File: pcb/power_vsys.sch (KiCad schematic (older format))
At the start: 36 parts

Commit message: Stephanie fixes, net names
Removed duplicate global I2C pull-ups
Added missing BMP280 pin 7
Correcting pin names etc. on LM4120 voltage reference
Finished standardizing net names
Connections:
- net labels added: 12Vout, LM5141-AGND, LM5141-VCC, LM5141-VDDA, VLogic, VSys-En, Vin
- net labels removed: 12VOUT, LM5141_AGND, LM5141_VCC, LM5141_VDDA, VIN, VLOGIC, VSYS_EN
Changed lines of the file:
@@
 12.5-16.8V IN
 Text HLabel 2750 1350 0    50   Input ~ 0
-VIN
+Vin
 Text HLabel 8700 1350 2    50   Output ~ 0
-12VOUT
+12Vout
 Wire Wire Line
 	8400 1350 8700 1350
@@
 	5250 1800 5750 1800
 Text Label 5750 1800 2    50   ~ 0
-LM5141_VCC
+LM5141-VCC
 Text Label 7700 4200 2    50   ~ 0
-LM5141_VCC
+LM5141-VCC
 Wire Wire Line
 	6450 4200 8050 4200
@@
 	7750 3600 8100 3600
 Text HLabel 8100 3600 2    50   Input ~ 0
-VLOGIC
+VLogic
 Wire Wire Line
 	7750 3900 8100 3900
@@
 	7150 4900 7150 5100
 Text Label 7250 4400 2    50   ~ 0
-LM5141_VDDA
+LM5141-VDDA
 $Comp
 L Device:R R?
@@
 $EndComp
 Text Label 6450 4700 0    50   ~ 0
-LM5141_AGND
+LM5141-AGND
 Wire Wire Line
 	6450 4900 7150 4900
@@
 	2150 4200 2150 5400
 Text Label 1200 5400 0    50   ~ 0
-LM5141_AGND
+LM5141-AGND
 Wire Wire Line
 	3150 4600 3150 5400
@@
 	2150 3500 2150 3600
 Text Label 1350 3500 0    50   ~ 0
-LM5141_VDDA
+LM5141-VDDA
 Wire Wire Line
 	2150 3500 1350 3500
@@
 	2700 3100 2300 3100
 Text HLabel 1350 3100 0    50   Input ~ 0
-VSYS_EN
+VSys-En
 $Comp
 L Device:R R?

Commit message: Diode symbol
Changed Schottky (BAT54J) from Diode library to Device library symbol
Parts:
- D?: symbol Diode:BAT54J -> Device:D_Schottky
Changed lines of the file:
@@
 	6450 4400 7450 4400
 $Comp
-L Diode:BAT54J D?
+L Device:D_Schottky D?
 U 1 1 6028E91B
 P 5100 1800

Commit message: Symbols
Re-assigned transistor symbols to Device:* and RespiraWorks_Std:*
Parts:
- Q?: symbol Transistor_BJT:MMBT3904 -> Device:Q_NPN_BCE
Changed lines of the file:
@@
 	3750 3500 3750 2500
 $Comp
-L Transistor_BJT:MMBT3904 Q?
+L Device:Q_NPN_BCE Q?
 U 1 1 602A3DA2
 P 2900 3100

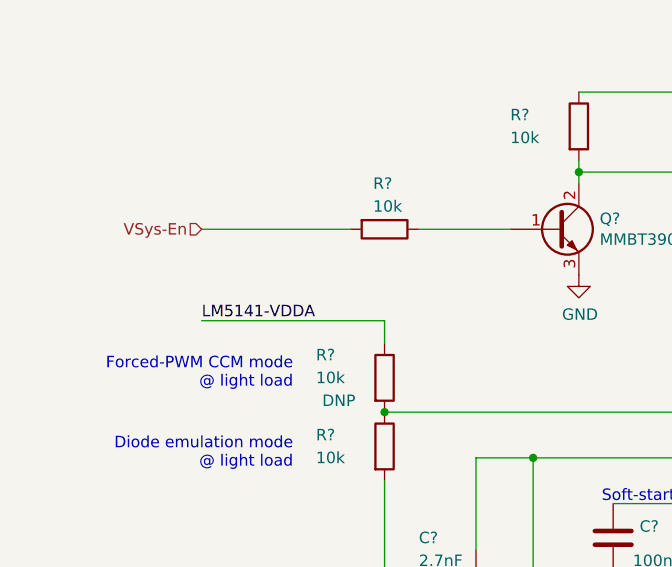
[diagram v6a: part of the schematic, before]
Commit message: Added VSys-Power-Off connection to FPGA
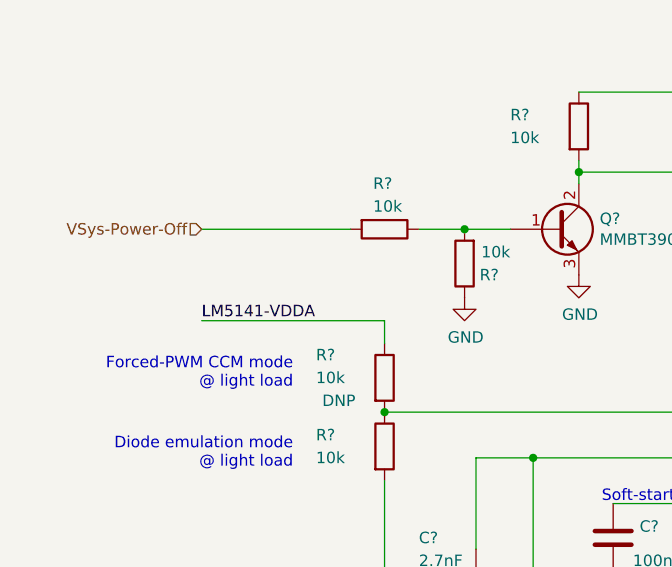
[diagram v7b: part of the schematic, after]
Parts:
- added R?: 10k, RespiraWorks_Std:R_0603_1608Metric, symbol Device:R
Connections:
- net labels added: VSys-Power-Off
- net labels removed: VSys-En
- wire segments 102 -> 103
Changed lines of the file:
@@
 	3750 3500 5000 3500
 Wire Wire Line
-	2700 3100 2300 3100
+	2700 3100 2500 3100
 Text HLabel 1350 3100 0    50   Input ~ 0
-VSys-En
+VSys-Power-Off
 $Comp
 L Device:R R?
@@
 Text Notes 7400 3100 0    50   ~ 0
 Regulates @ FB = 1.2V;\nNom. 12.1V out
+$Comp
+L Device:R R?
+U 1 1 6058DDDE
+P 2500 3250
+AR Path="/601A64F8/6058DDDE" Ref="R?"  Part="1"
+AR Path="/601A64F8/60567144/6058DDDE" Ref="R?"  Part="1"
+AR Path="/601A64F8/60567D6E/6058DDDE" Ref="R?"  Part="1"
+AR Path="/6023BF6A/60567D6E/6058DDDE" Ref="R?"  Part="1"
+AR Path="/6041384A/60567D6E/6058DDDE" Ref="R?"  Part="1"
+F 0 "R?" H 2350 3300 50  0000 L CNN
+F 1 "10k" H 2300 3200 50  0000 L CNN
+F 2 "RespiraWorks_Std:R_0603_1608Metric" V 2430 3250 50  0001 C CNN
+F 3 "~" H 2500 3250 50  0001 C CNN
+	1    2500 3250
+	-1   0    0    1
+$EndComp
+Connection ~ 2500 3100
+Wire Wire Line
+	2500 3100 2300 3100
+$Comp
+L power:GND #PWR?
+U 1 1 6058E3DA
+P 2500 3400
+AR Path="/601A64F8/6058E3DA" Ref="#PWR?"  Part="1"
+AR Path="/601A64F8/60567144/6058E3DA" Ref="#PWR?"  Part="1"
+AR Path="/601A64F8/60567D6E/6058E3DA" Ref="#PWR?"  Part="1"
+AR Path="/6023BF6A/60567D6E/6058E3DA" Ref="#PWR?"  Part="1"
+AR Path="/6041384A/60567D6E/6058E3DA" Ref="#PWR?"  Part="1"
+F 0 "#PWR?" H 2500 3150 50  0001 C CNN
+F 1 "GND" H 2505 3227 50  0000 C CNN
+F 2 "" H 2500 3400 50  0001 C CNN
+F 3 "" H 2500 3400 50  0001 C CNN
+	1    2500 3400
+	1    0    0    -1
+$EndComp
 $EndSCHEMATC

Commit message: update to alt parts in the VSYS (LM5141) buck
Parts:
- Q? (x2): value CSD17304Q3 -> BSZ019N03LSATMA1; footprint RespiraWorks_Std:VSON-8_3.3x3.3mm_P0.65mm_NexFET -> RespiraWorks:VSON-8-SGD_3.3x3.3mm_P0.65mm_NexFET; symbol RespiraWorks_Std:CSD17304Q3 -> RespiraWorks_Std:Q_NMOS_SGD; Manufacturer Texas Instruments -> Infineon; Manufacturer PN CSD17304Q3 -> BSZ019N03LSATMA1
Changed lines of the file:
@@
 Connection ~ 4950 1350
 $Comp
-L RespiraWorks_Std:CSD17304Q3 Q?
+L RespiraWorks_Std:Q_NMOS_SGD Q?
 U 1 1 601DFE01
 P 4400 1550
@@
 AR Path="/6023BF6A/60567D6E/601DFE01" Ref="Q?"  Part="1"
 AR Path="/6041384A/60567D6E/601DFE01" Ref="Q?"  Part="1"
-F 0 "Q?" H 4450 1950 50  0000 L CNN
-F 1 "CSD17304Q3" H 4300 1850 50  0000 L CNN
-F 2 "RespiraWorks_Std:VSON-8_3.3x3.3mm_P0.65mm_NexFET" H 4600 1475 50  0001 L CIN
-F 3 "https://www.ti.com/lit/ds/symlink/csd17304q3.pdf?ts=1608773956037" V 4400 1550 50  0001 L CNN
-F 4 "Texas Instruments" H 4400 1550 50  0001 C CNN "Manufacturer"
-F 5 "CSD17304Q3" H 4400 1550 50  0001 C CNN "Manufacturer PN"
+F 0 "Q?" H 4550 1950 50  0000 L CNN
+F 1 "BSZ019N03LSATMA1" H 4300 1850 50  0000 L CNN
+F 2 "RespiraWorks:VSON-8-SGD_3.3x3.3mm_P0.65mm_NexFET" H 4600 1475 50  0001 L CIN
+F 3 "https://www.infineon.com/dgdl/BSZ019N03LS_Rev+2.1.pdf?folderId=db3a304326dfb1300126fb3bec803f1a&fileId=db3a304326dfb1300126fb7ddf173f4e" V 4400 1550 50  0001 L CNN
+F 4 "Infineon" H 4400 1550 50  0001 C CNN "Manufacturer"
+F 5 "BSZ019N03LSATMA1" H 4400 1550 50  0001 C CNN "Manufacturer PN"
 	1    4400 1550
 	1    0    0    -1
@@
 Connection ~ 4700 1350
 $Comp
-L RespiraWorks_Std:CSD17304Q3 Q?
+L RespiraWorks_Std:Q_NMOS_SGD Q?
 U 1 1 601DFDDC
 P 4050 1450
@@
 AR Path="/6023BF6A/60567D6E/601DFDDC" Ref="Q?"  Part="1"
 AR Path="/6041384A/60567D6E/601DFDDC" Ref="Q?"  Part="1"
-F 0 "Q?" V 4450 1450 50  0000 C CNN
-F 1 "CSD17304Q3" V 4350 1500 50  0000 C CNN
-F 2 "RespiraWorks_Std:VSON-8_3.3x3.3mm_P0.65mm_NexFET" H 4250 1375 50  0001 L CIN
-F 3 "https://www.ti.com/lit/ds/symlink/csd17304q3.pdf?ts=1608773956037" V 4050 1450 50  0001 L CNN
-F 4 "Texas Instruments" H 4050 1450 50  0001 C CNN "Manufacturer"
-F 5 "CSD17304Q3" H 4050 1450 50  0001 C CNN "Manufacturer PN"
+F 0 "Q?" V 4500 1450 50  0000 C CNN
+F 1 "BSZ019N03LSATMA1" V 4400 1450 50  0000 C CNN
+F 2 "RespiraWorks:VSON-8-SGD_3.3x3.3mm_P0.65mm_NexFET" H 4250 1375 50  0001 L CIN
+F 3 "https://www.infineon.com/dgdl/BSZ019N03LS_Rev+2.1.pdf?folderId=db3a304326dfb1300126fb3bec803f1a&fileId=db3a304326dfb1300126fb7ddf173f4e" V 4050 1450 50  0001 L CNN
+F 4 "Infineon" H 4050 1450 50  0001 C CNN "Manufacturer"
+F 5 "BSZ019N03LSATMA1" H 4050 1450 50  0001 C CNN "Manufacturer PN"
 	1    4050 1450
 	0    -1   -1   0
